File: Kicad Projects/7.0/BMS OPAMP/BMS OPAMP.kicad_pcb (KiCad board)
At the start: 2 copper layers, 85.1 x 85.1 mm, 136 parts, among them J1 CHG/DSCHG CTRL, J2 CHG/DSCHG CTRL CMP (SHORT DAT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, J3 Data IN/OUT, J4 Data IN/OUT, J5 Port Selector, J6 Port Selector, J7 NTC1, J8 NTC2, J9 Balance Connector, Q1 MMBT3906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

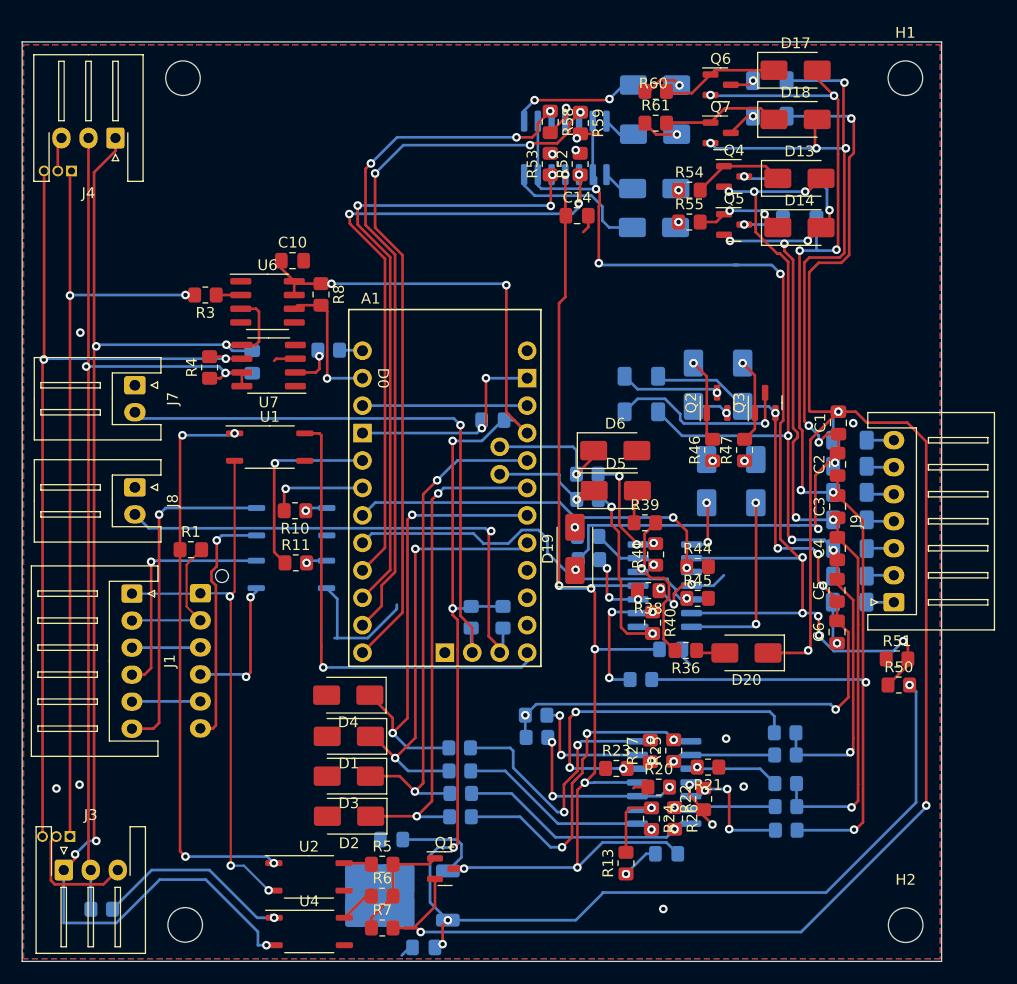
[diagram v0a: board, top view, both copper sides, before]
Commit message: Ordered pcbs for bms
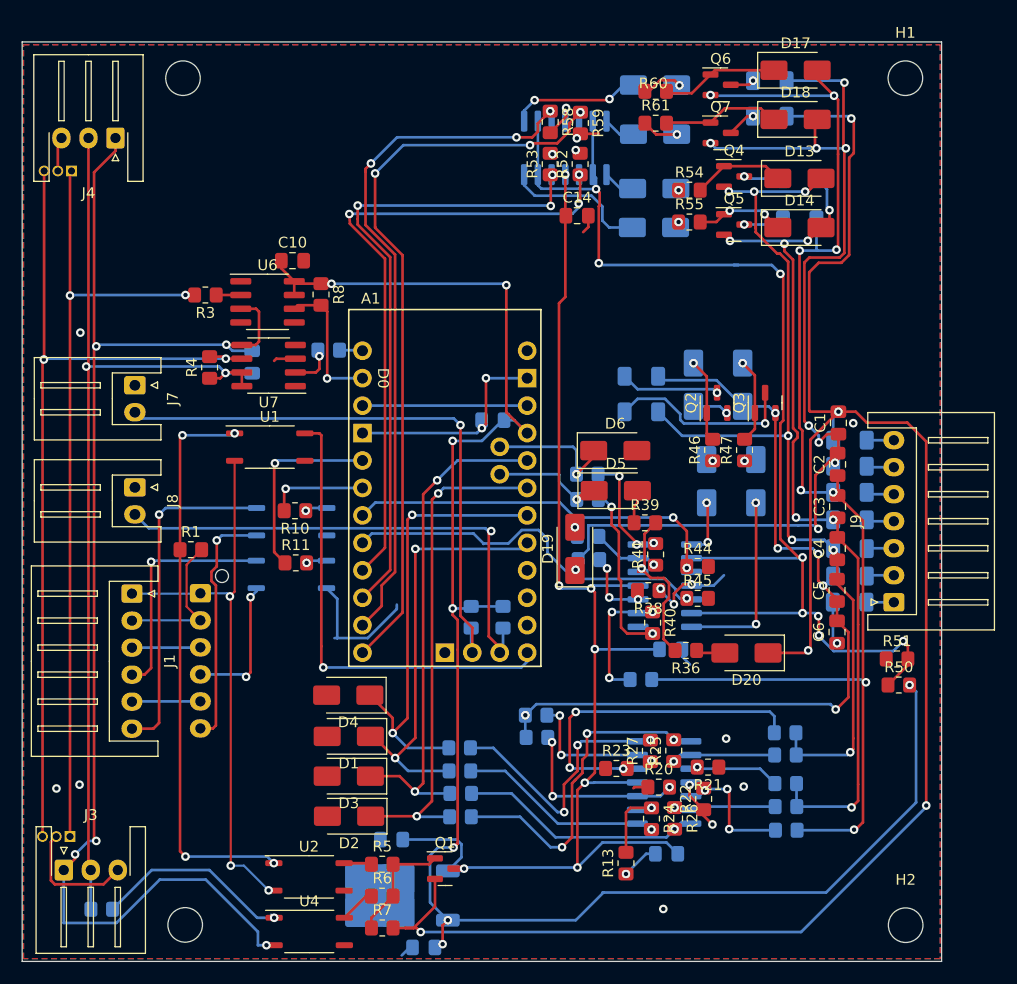
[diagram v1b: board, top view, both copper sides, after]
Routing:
- net Net-(R27-Pad2): track 25.7 -> 24.8 mm

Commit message: IDEK
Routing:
- net B0: vias 21 -> 18
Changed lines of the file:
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@@
   )
   (setup
+    (stackup
+      (layer "F.SilkS" (type "Top Silk Screen"))
+      (layer "F.Paste" (type "Top Solder Paste"))
+      (layer "F.Mask" (type "Top Solder Mask") (thickness 0.01))
+      (layer "F.Cu" (type "copper") (thickness 0.035))
+      (layer "dielectric 1" (type "core") (thickness 1.51) (material "FR4") (epsilon_r 4.5) (loss_tangent 0.02))
+      (layer "B.Cu" (type "copper") (thickness 0.035))
+      (layer "B.Mask" (type "Bottom Solder Mask") (thickness 0.01))
+      (layer "B.Paste" (type "Bottom Solder Paste"))
+      (layer "B.SilkS" (type "Bottom Silk Screen"))
+      (copper_finish "None")
+      (dielectric_constraints no)
+    )
     (pad_to_mask_clearance 0)
     (pcbplotparams
@@
   (via (at 99.3902 51.0286) (size 0.8) (drill 0.4) (layers "F.Cu" "B.Cu") (free) (net 23))
   (via (at 81.5594 66.3448) (size 0.8) (drill 0.4) (layers "F.Cu" "B.Cu") (net 23))
-  (via (at 25.654 84.836) (size 0.8) (drill 0.4) (layers "F.Cu" "B.Cu") (free) (net 23))
   (via (at 87.6579 50.0865) (size 0.8) (drill 0.4) (layers "F.Cu" "B.Cu") (net 23))
   (via (at 73.7102 25.7556) (size 0.8) (drill 0.4) (layers "F.Cu" "B.Cu") (net 23))
@@
   (via (at 89.2556 84.6582) (size 0.8) (drill 0.4) (layers "F.Cu" "B.Cu") (free) (net 23))
   (via (at 86.36 88.1634) (size 0.8) (drill 0.4) (layers "F.Cu" "B.Cu") (net 23))
-  (via (at 27.7876 84.4804) (size 0.8) (drill 0.4) (layers "F.Cu" "B.Cu") (free) (net 23))
   (via (at 73.8118 24.6634) (size 0.8) (drill 0.4) (layers "F.Cu" "B.Cu") (net 23))
   (via (at 87.628682 80.218741) (size 0.8) (drill 0.4) (layers "F.Cu" "B.Cu") (free) (net 23))
@@
   (via (at 78.359 92.7448) (size 0.8) (drill 0.4) (layers "F.Cu" "B.Cu") (net 23))
   (via (at 82.794362 67.789337) (size 0.8) (drill 0.4) (layers "F.Cu" "B.Cu") (net 23))
-  (via (at 27.8638 42.6466) (size 0.8) (drill 0.4) (layers "F.Cu" "B.Cu") (free) (net 23))
   (via (at 71.5512 26.1366) (size 0.8) (drill 0.4) (layers "F.Cu" "B.Cu") (net 23))
   (via (at 72.8212 21.8595) (size 0.8) (drill 0.4) (layers "F.Cu" "B.Cu") (net 23))

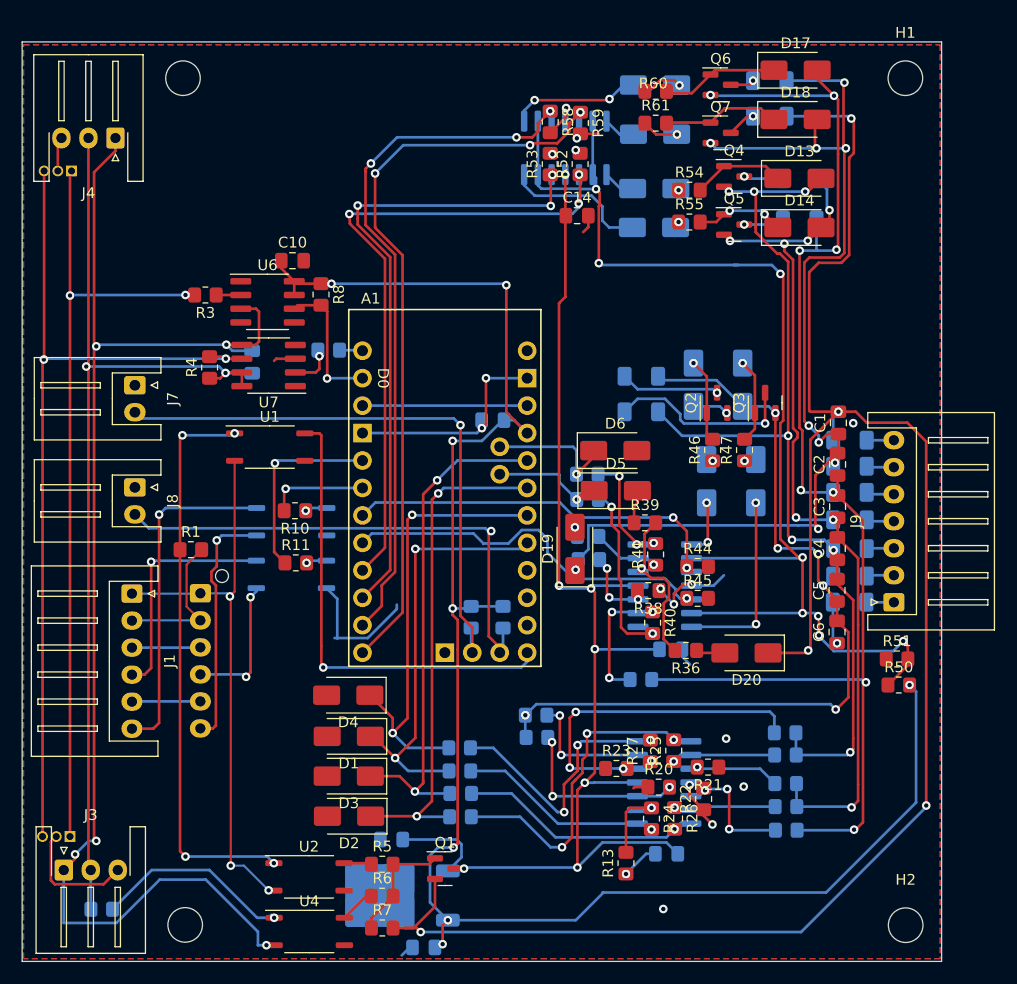
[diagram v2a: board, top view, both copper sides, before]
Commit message: IDEK but LTC6804 Ordered
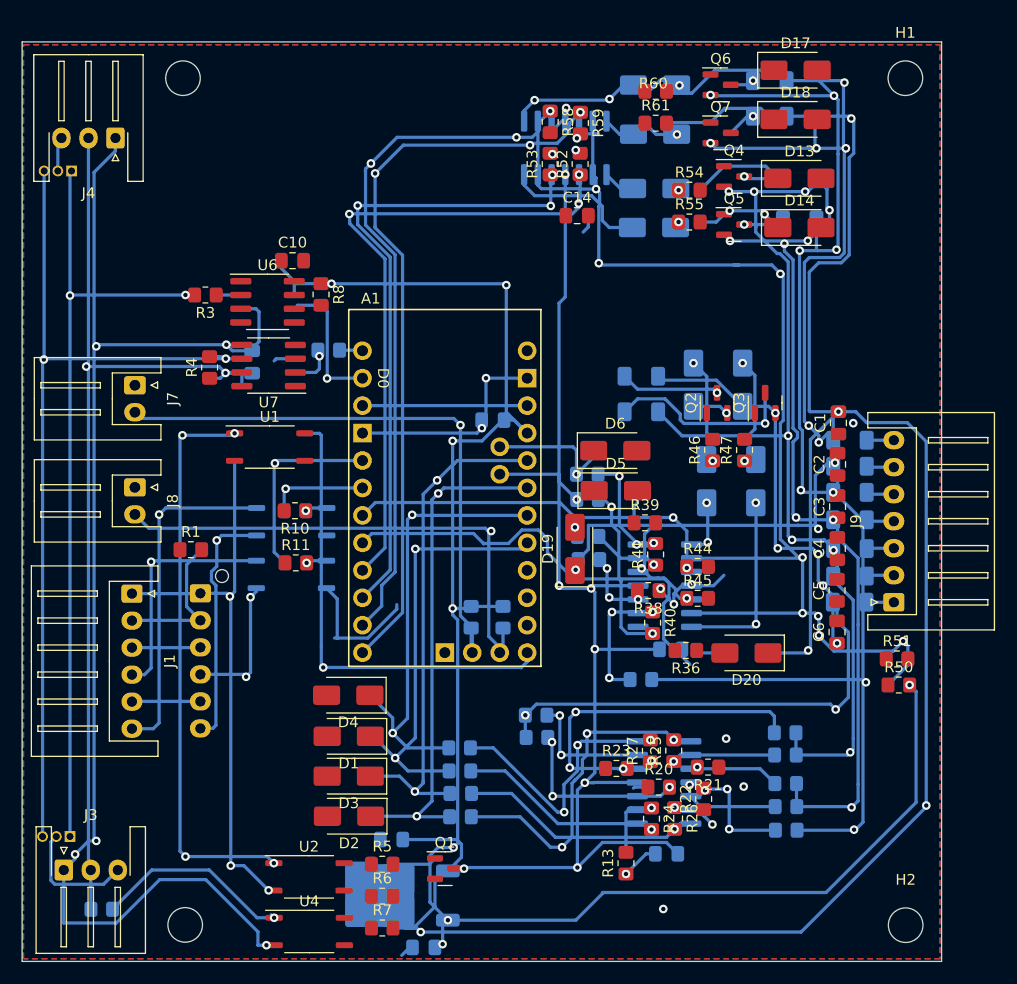
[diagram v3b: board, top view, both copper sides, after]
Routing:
- net Net-(Q4-C): track 3.67 -> 12.2 mm
- net Net-(D13-K): track 8.58 -> 0.00 mm
